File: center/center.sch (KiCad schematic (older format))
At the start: 48 parts, among them J1 top left, J2 top right, J3 bottom left, J4 bottom right, J5 SWD, Q1 AO3400, Q2 IRLML6402, Q3 AO3400, Q4 AO3400, Q5 IRLML6402, U1 AP1117-33, U2 STM32F030F4P6, Y1 8MHz

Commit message: PCB designs R01 finished (not reviewed yet)
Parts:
- added TP1, TP2, TP3, TP4: TestPoint, Measurement_Points:Measurement_Point_Square-SMD-Pad_Small, symbol Connector:TestPoint
- C1, C4: footprint (none) -> Capacitor_THT:CP_Radial_D10.0mm_P5.00mm
- C10, C2, C3, C5, C6, C7, C8, C9: footprint (none) -> Capacitors_SMD:C_0603_HandSoldering
- C11, C12, C13: footprint (none) -> Capacitors_SMD:C_0805
- D1, D2, D3, D4: footprint (none) -> Diodes_SMD:D_SMB_Handsoldering
- D5, D6, D7, D8: footprint (none) -> Diodes_SMD:D_MiniMELF_Handsoldering
- J1, J2: footprint (none) -> footprints:led_tape_3528_2835
- J3: value bottom left -> bottom right; footprint (none) -> footprints:led_tape_3528_2835
- J4: value bottom right -> bottom left; footprint (none) -> footprints:led_tape_3528_2835
- J5: footprint (none) -> Pin_Headers:Pin_Header_Straight_1x04_Pitch2.54mm
- Q1, Q3, Q4: footprint Package_DirectFET:DirectFET_S1 -> TO_SOT_Packages_SMD:SOT-23
- Q2, Q5: footprint Package_TO_SOT_SMD:SOT-23 -> TO_SOT_Packages_SMD:SOT-23
- R1, R11, R12, R13, R14, R2, R3, R4, R5, R6, R7, R8, R9: footprint (none) -> Resistors_SMD:R_0603_HandSoldering
- R10: footprint (none) -> Resistors_SMD:R_2512_HandSoldering
- U1: footprint Package_TO_SOT_SMD:SOT-223-3_TabPin2 -> TO_SOT_Packages_SMD:SOT-223-3Lead_TabPin2
- U2: footprint Package_SO:TSSOP-20_4.4x6.5mm_P0.65mm -> Housings_SSOP:TSSOP-20_4.4x6.5mm_Pitch0.65mm
- Y1: footprint (none) -> Crystals:Crystal_SMD_3225-4pin_3.2x2.5mm
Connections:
- net CH1: now also U2.13 (PA7); no longer U2.10 (PA4)
- net CH3: now also U2.10 (PA4); no longer U2.13 (PA7)
- net at U2.11 (PA5): now also TP1.1
- net at U2.14 (PB1): now also TP4.1
- net at U2.17 (PA9): now also TP2.1
- net at U2.18 (PA10): now also TP3.1
- net at C9.1, Y1.1: now also U2.3 (PF1); no longer U2.2 (PF0)
- net at C10.1, Y1.3: now also U2.2 (PF0); no longer U2.3 (PF1)

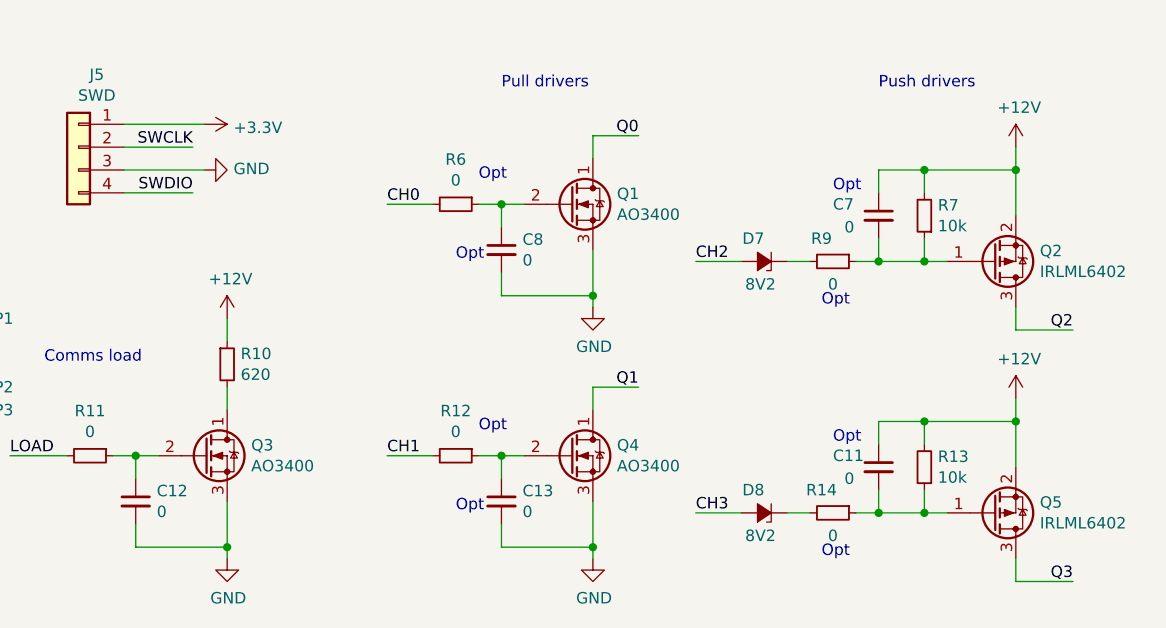
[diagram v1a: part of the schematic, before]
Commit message: Fix AO3400 pinout
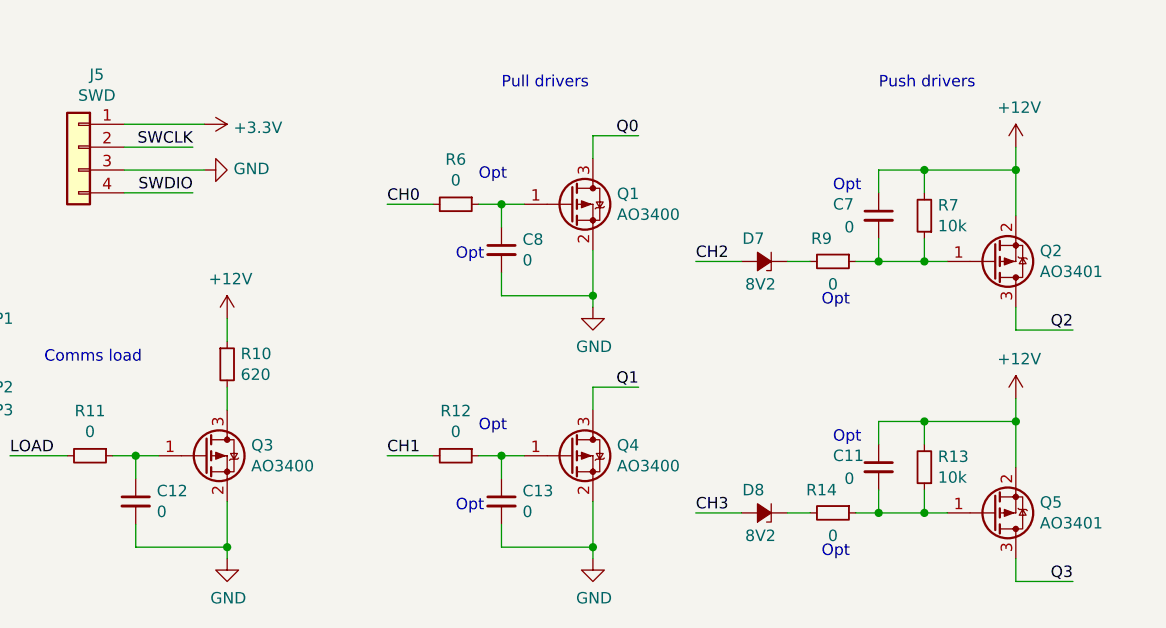
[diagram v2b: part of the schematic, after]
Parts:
- removed Q1, Q3, Q4: AO3400, TO_SOT_Packages_SMD:SOT-23, symbol Transistor_FET:IRF6710S2
- added Q1, Q3, Q4: AO3400, Package_TO_SOT_SMD:SOT-23, symbol Transistor_FET:BSS83P
- Q2, Q5: value IRLML6402 -> AO3401
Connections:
- net GND: now also Q1.2 (S), Q3.2 (S), Q4.2 (S)
- net Q0: now also Q1.3 (D)
- net Q1: now also Q4.3 (D)
- net at R10.2: now also Q3.3 (D)
- net at C12.1, R11.1: now also Q3.1 (G)
- net at C13.1, R12.1: now also Q4.1 (G)
- net at C8.1, R6.1: now also Q1.1 (G)
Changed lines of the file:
@@
 EESchema Schematic File Version 4
+LIBS:center-cache
 EELAYER 26 0
 EELAYER END
@@
 	3800 4450 4200 4450
 $Comp
-L Transistor_FET:IRF6710S2 Q3
-U 1 1 5C1F9130
-P 5250 5450
-F 0 "Q3" H 5455 5496 50  0000 L CNN
-F 1 "AO3400" H 5455 5405 50  0000 L CNN
-F 2 "TO_SOT_Packages_SMD:SOT-23" H 5250 5450 50  0001 C CIN
-F 3 "https://www.infineon.com/dgdl/irf6710s2pbf.pdf?fileId=5546d462533600a4015355ece3db1a78" H 5250 5450 50  0001 L CNN
-	1    5250 5450
-	1    0    0    -1
-$EndComp
-$Comp
 L Device:R_Small R10
 U 1 1 5C1F9EE6
@@
 LOAD
 $Comp
-L Transistor_FET:IRF6710S2 Q4
-U 1 1 5C24FD36
-P 6850 5450
-F 0 "Q4" H 7055 5496 50  0000 L CNN
-F 1 "AO3400" H 7055 5405 50  0000 L CNN
-F 2 "TO_SOT_Packages_SMD:SOT-23" H 6850 5450 50  0001 C CIN
-F 3 "https://www.infineon.com/dgdl/irf6710s2pbf.pdf?fileId=5546d462533600a4015355ece3db1a78" H 6850 5450 50  0001 L CNN
-	1    6850 5450
-	1    0    0    -1
-$EndComp
-$Comp
 L power:GND #PWR0108
 U 1 1 5C24FD42
@@
 	7150 5150 6950 5150
 $Comp
-L Transistor_FET:IRF6710S2 Q1
-U 1 1 5C265A5A
-P 6850 4350
-F 0 "Q1" H 7055 4396 50  0000 L CNN
-F 1 "AO3400" H 7055 4305 50  0000 L CNN
-F 2 "TO_SOT_Packages_SMD:SOT-23" H 6850 4350 50  0001 C CIN
-F 3 "https://www.infineon.com/dgdl/irf6710s2pbf.pdf?fileId=5546d462533600a4015355ece3db1a78" H 6850 4350 50  0001 L CNN
-	1    6850 4350
-	1    0    0    -1
-$EndComp
-$Comp
 L power:GND #PWR0109
 U 1 1 5C265A60
@@
 P 8700 4600
 F 0 "Q2" H 8905 4554 50  0000 L CNN
-F 1 "IRLML6402" H 8905 4645 50  0000 L CNN
+F 1 "AO3401" H 8905 4645 50  0000 L CNN
 F 2 "TO_SOT_Packages_SMD:SOT-23" H 8900 4525 50  0001 L CIN
 F 3 "https://www.infineon.com/dgdl/irlml6402pbf.pdf?fileId=5546d462533600a401535668d5c2263c" H 8700 4600 50  0001 L CNN
@@
 P 8700 5700
 F 0 "Q5" H 8905 5654 50  0000 L CNN
-F 1 "IRLML6402" H 8905 5745 50  0000 L CNN
+F 1 "AO3401" H 8905 5745 50  0000 L CNN
 F 2 "TO_SOT_Packages_SMD:SOT-23" H 8900 5625 50  0001 L CIN
 F 3 "https://www.infineon.com/dgdl/irlml6402pbf.pdf?fileId=5546d462533600a401535668d5c2263c" H 8700 5700 50  0001 L CNN
@@
 Wire Wire Line
 	2600 5150 2600 5300
+$Comp
+L Transistor_FET:BSS83P Q1
+U 1 1 5C577582
+P 6850 4350
+F 0 "Q1" H 7055 4396 50  0000 L CNN
+F 1 "AO3400" H 7055 4305 50  0000 L CNN
+F 2 "Package_TO_SOT_SMD:SOT-23" H 7050 4275 50  0001 L CIN
+F 3 "http://www.farnell.com/datasheets/1835997.pdf" H 6850 4350 50  0001 L CNN
+	1    6850 4350
+	1    0    0    -1
+$EndComp
+$Comp
+L Transistor_FET:BSS83P Q3
+U 1 1 5C57CF20
+P 5250 5450
+F 0 "Q3" H 5455 5496 50  0000 L CNN
+F 1 "AO3400" H 5455 5405 50  0000 L CNN
+F 2 "Package_TO_SOT_SMD:SOT-23" H 5450 5375 50  0001 L CIN
+F 3 "http://www.farnell.com/datasheets/1835997.pdf" H 5250 5450 50  0001 L CNN
+	1    5250 5450
+	1    0    0    -1
+$EndComp
+$Comp
+L Transistor_FET:BSS83P Q4
+U 1 1 5C57D930
+P 6850 5450
+F 0 "Q4" H 7055 5496 50  0000 L CNN
+F 1 "AO3400" H 7055 5405 50  0000 L CNN
+F 2 "Package_TO_SOT_SMD:SOT-23" H 7050 5375 50  0001 L CIN
+F 3 "http://www.farnell.com/datasheets/1835997.pdf" H 6850 5450 50  0001 L CNN
+	1    6850 5450
+	1    0    0    -1
+$EndComp
 $EndSCHEMATC

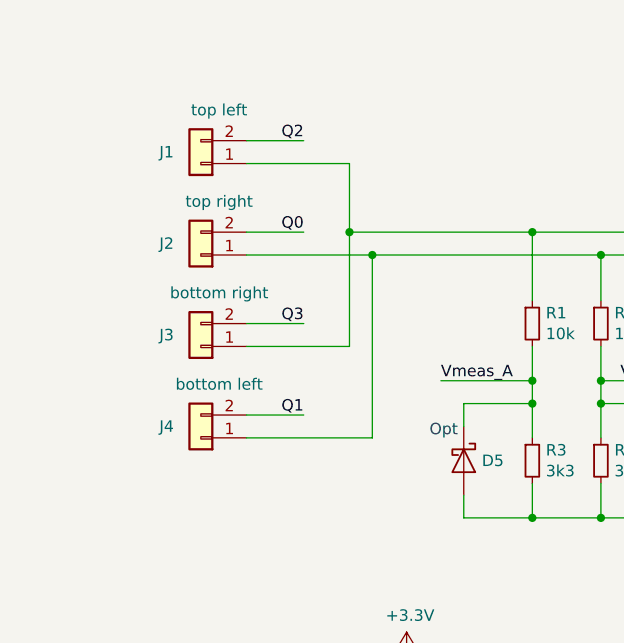
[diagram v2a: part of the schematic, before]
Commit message: center: fix tape footprint polarity, vcc short, silk
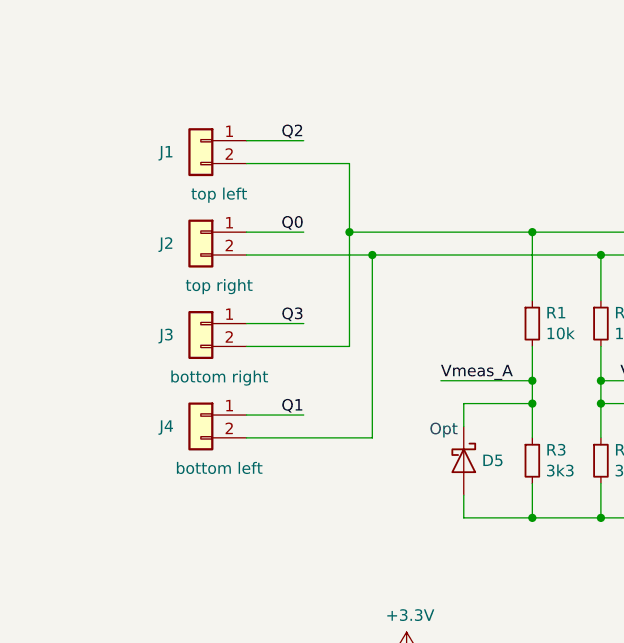
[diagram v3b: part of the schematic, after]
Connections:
- net Q0: now also J2.1 (Pin_1); no longer J2.2 (Pin_2)
- net Q1: now also J4.1 (Pin_1); no longer J4.2 (Pin_2)
- net Q2: now also J1.1 (Pin_1); no longer J1.2 (Pin_2)
- net Q3: now also J3.1 (Pin_1); no longer J3.2 (Pin_2)
- net at D1.2 (A), D3.1 (K), R1.1: now also J1.2 (Pin_2), J3.2 (Pin_2); no longer J1.1 (Pin_1), J3.1 (Pin_1)
- net at D2.2 (A), D4.1 (K), R2.1: now also J2.2 (Pin_2), J4.2 (Pin_2); no longer J2.1 (Pin_1), J4.1 (Pin_1)
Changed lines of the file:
@@
 L Connector_Generic:Conn_01x02 J1
 U 1 1 5C196961
-P 2500 1800
-F 0 "J1" H 2650 1750 50  0000 C CNN
-F 1 "top left" H 2420 1566 50  0000 C CNN
-F 2 "footprints:led_tape_3528_2835" H 2500 1800 50  0001 C CNN
-F 3 "~" H 2500 1800 50  0001 C CNN
-	1    2500 1800
-	-1   0    0    1
+P 2500 1700
+F 0 "J1" H 2650 1650 50  0000 C CNN
+F 1 "top left" H 2420 1466 50  0000 C CNN
+F 2 "footprints:led_tape_3528_2835" H 2500 1700 50  0001 C CNN
+F 3 "~" H 2500 1700 50  0001 C CNN
+	1    2500 1700
+	-1   0    0    -1
 $EndComp
 $Comp
 L Connector_Generic:Conn_01x02 J2
 U 1 1 5C196B9D
-P 2500 2200
-F 0 "J2" H 2650 2150 50  0000 C CNN
-F 1 "top right" H 2420 1966 50  0000 C CNN
-F 2 "footprints:led_tape_3528_2835" H 2500 2200 50  0001 C CNN
-F 3 "~" H 2500 2200 50  0001 C CNN
-	1    2500 2200
-	-1   0    0    1
+P 2500 2100
+F 0 "J2" H 2650 2050 50  0000 C CNN
+F 1 "top right" H 2420 1866 50  0000 C CNN
+F 2 "footprints:led_tape_3528_2835" H 2500 2100 50  0001 C CNN
+F 3 "~" H 2500 2100 50  0001 C CNN
+	1    2500 2100
+	-1   0    0    -1
 $EndComp
 $Comp
 L Connector_Generic:Conn_01x02 J3
 U 1 1 5C196C4D
-P 2500 2600
-F 0 "J3" H 2650 2550 50  0000 C CNN
-F 1 "bottom right" H 2420 2366 50  0000 C CNN
-F 2 "footprints:led_tape_3528_2835" H 2500 2600 50  0001 C CNN
-F 3 "~" H 2500 2600 50  0001 C CNN
-	1    2500 2600
-	-1   0    0    1
+P 2500 2500
+F 0 "J3" H 2650 2450 50  0000 C CNN
+F 1 "bottom right" H 2420 2266 50  0000 C CNN
+F 2 "footprints:led_tape_3528_2835" H 2500 2500 50  0001 C CNN
+F 3 "~" H 2500 2500 50  0001 C CNN
+	1    2500 2500
+	-1   0    0    -1
 $EndComp
 $Comp
 L Connector_Generic:Conn_01x02 J4
 U 1 1 5C196D8E
-P 2500 3000
-F 0 "J4" H 2650 2950 50  0000 C CNN
-F 1 "bottom left" H 2420 2766 50  0000 C CNN
-F 2 "footprints:led_tape_3528_2835" H 2500 3000 50  0001 C CNN
-F 3 "~" H 2500 3000 50  0001 C CNN
-	1    2500 3000
-	-1   0    0    1
+P 2500 2900
+F 0 "J4" H 2650 2850 50  0000 C CNN
+F 1 "bottom left" H 2420 2666 50  0000 C CNN
+F 2 "footprints:led_tape_3528_2835" H 2500 2900 50  0001 C CNN
+F 3 "~" H 2500 2900 50  0001 C CNN
+	1    2500 2900
+	-1   0    0    -1
 $EndComp
 $Comp
